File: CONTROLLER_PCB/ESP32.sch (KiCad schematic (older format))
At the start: 6 parts

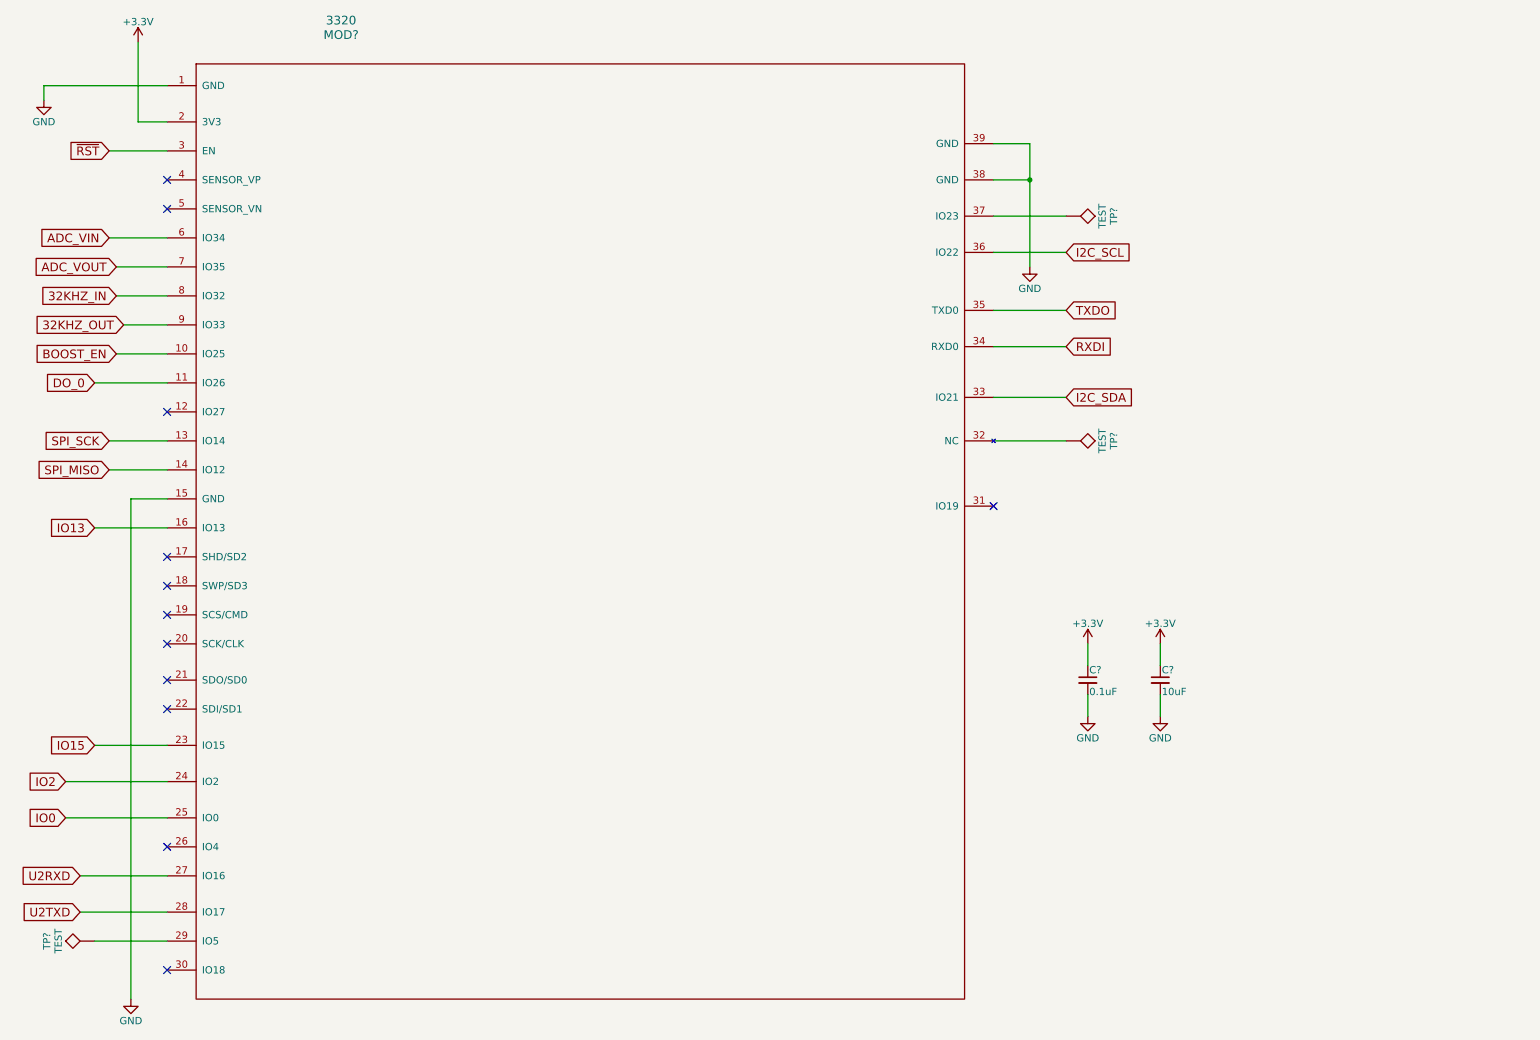
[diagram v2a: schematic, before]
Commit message: Finalized schematic, created BOM, started placement (no PCB size yet)
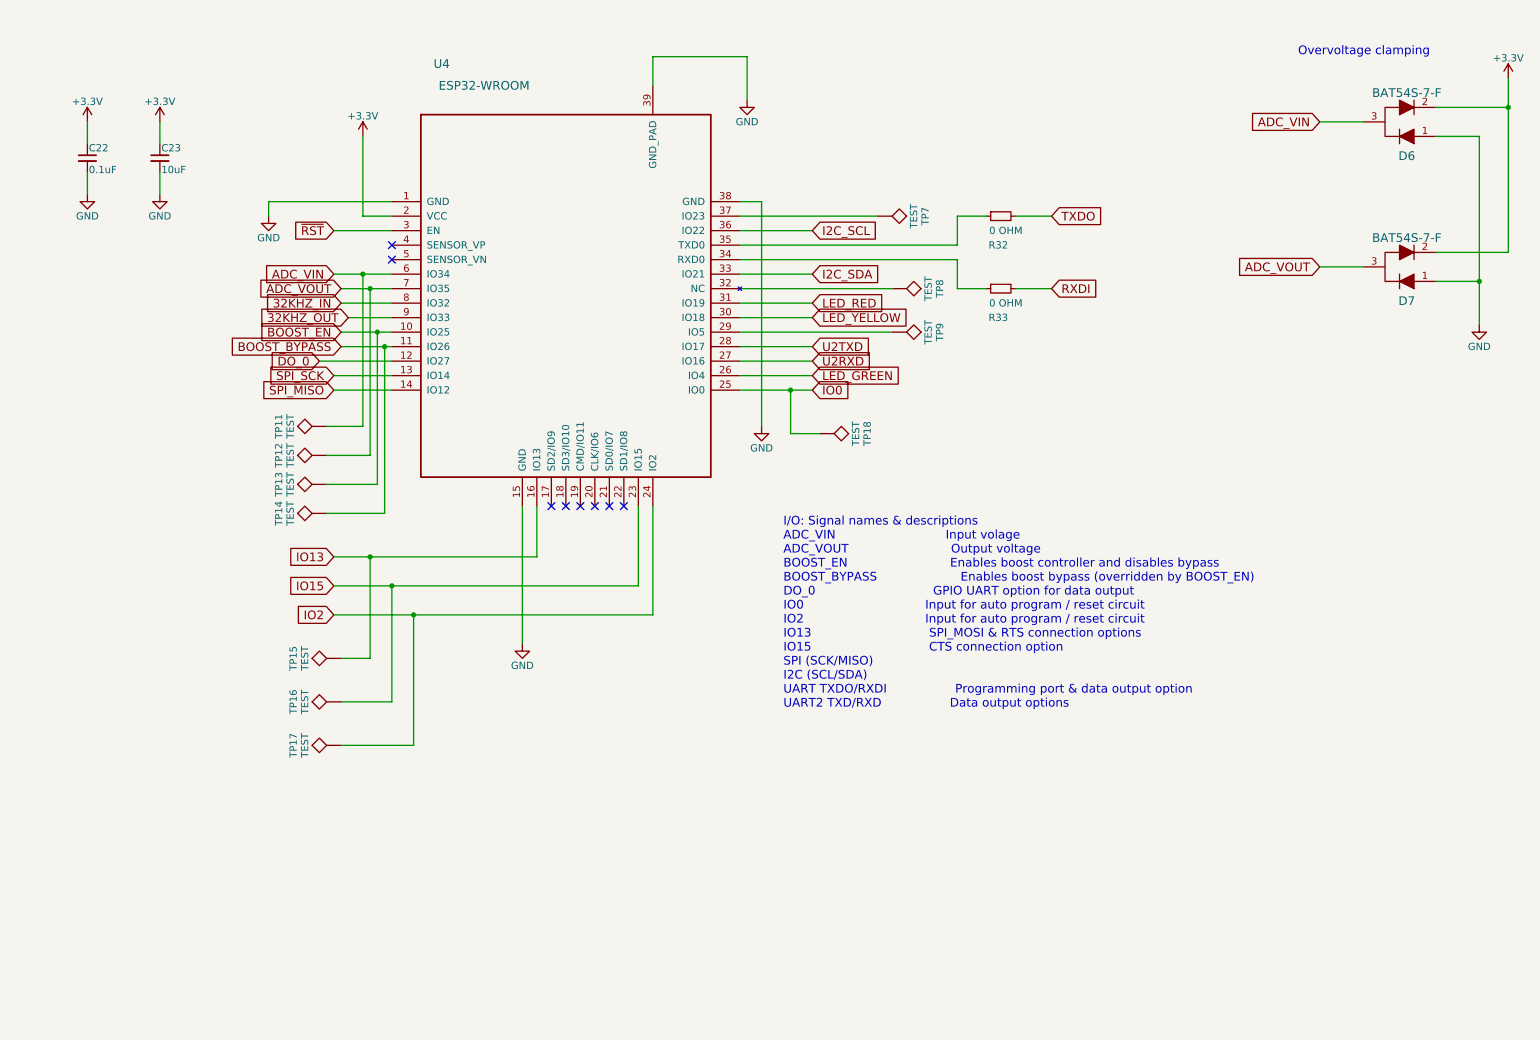
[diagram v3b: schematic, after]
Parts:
- removed MOD?: 3320, digikey-footprints:None, symbol 3320
- removed TP? (x3): TEST, Measurement_Points:Measurement_Point_Round-SMD-Pad_Small, symbol TEST
- added D6, D7: BAT54S-7-F, digikey-footprints:SOT-23-3, symbol BAT54S-7-F
- added R32, R33: 0 OHM, Resistors_SMD:R_0603_HandSoldering, symbol R_Small
- added TP11, TP12, TP13, TP14, TP15, TP16, TP17, TP18, TP7, TP8, TP9: TEST, Measurement_Points:Measurement_Point_Round-SMD-Pad_Small, symbol TEST
- added U4: ESP32-WROOM, ESP32-footprints-Lib:ESP32-WROOM, symbol ESP32-WROOM
- gave numbers to parts that had none: 2
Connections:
- net +3V3: now also D6.2, D7.2, U4.2 (VCC)
- net 32KHZ_IN: now also U4.8 (IO32)
- net 32KHZ_OUT: now also U4.9 (IO33)
- net ADC_VIN: now also D6.3, TP11.1, U4.6 (IO34)
- net ADC_VOUT: now also D7.3, TP12.1, U4.7 (IO35)
- net BOOST_EN: now also TP13.1, U4.10 (IO25)
- net DO_0: now also U4.12 (IO27)
- net GND: now also D6.1, D7.1, U4.1 (GND), U4.15 (GND), U4.38 (GND), U4.39 (GND_PAD)
- net I2C_SCL: now also U4.36 (IO22)
- net I2C_SDA: now also U4.33 (IO21)
- net IO0: now also TP18.1, U4.25 (IO0)
- net IO13: now also TP15.1, U4.16 (IO13)
- net IO15: now also TP16.1, U4.23 (IO15)
- net IO2: now also TP17.1, U4.24 (IO2)
- net RXDI: now also R33.2
- net SPI_MISO: now also U4.14 (IO12)
- net SPI_SCK: now also U4.13 (IO14)
- net TXDO: now also R32.2
- net U2RXD: now also U4.27 (IO16)
- net U2TXD: now also U4.28 (IO17)
- net ~RST: now also U4.3 (EN)
- new net: TP9.1, U4.29 (IO5)
- new net: TP8.1, U4.32 (NC)
- new net: R33.1, U4.34 (RXD0)
- new net: R32.1, U4.35 (TXD0)
- new net: TP7.1, U4.37 (IO23)
- new net BOOST_BYPASS: TP14.1, U4.11 (IO26)
- new net LED_GREEN: U4.26 (IO4)
- new net LED_RED: U4.31 (IO19)
- new net LED_YELLOW: U4.30 (IO18)
- no-connect marks 12 -> 8
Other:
- note added: "I/O: Signal names & descriptions\nADC_VIN Input volage\nADC_VOUT Output voltage\nBOOST_EN Enables boost controller and disables bypass\nBOOST_BYPASS Enables boost bypass (overridden by BOOST_EN)\nDO_0 GPIO UART option for data output\nIO0 Input for auto program / reset circuit\nIO2 Input for auto program / reset circuit\nIO13 SPI_MOSI & RTS connection options\nIO15 CTS connection option\nSPI (SCK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"
- note added: "Overvoltage clamping"
- moved on the sheet: C22, C23
